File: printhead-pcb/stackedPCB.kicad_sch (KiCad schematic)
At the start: 17 parts, among them J13 Steckverbinder_Male_1, J14 Steckverbinder_Male_2, J15 Steckverbinder_Female_2, J16 Steckverbinder_Male_3, J17 Steckverbinder_Female_3

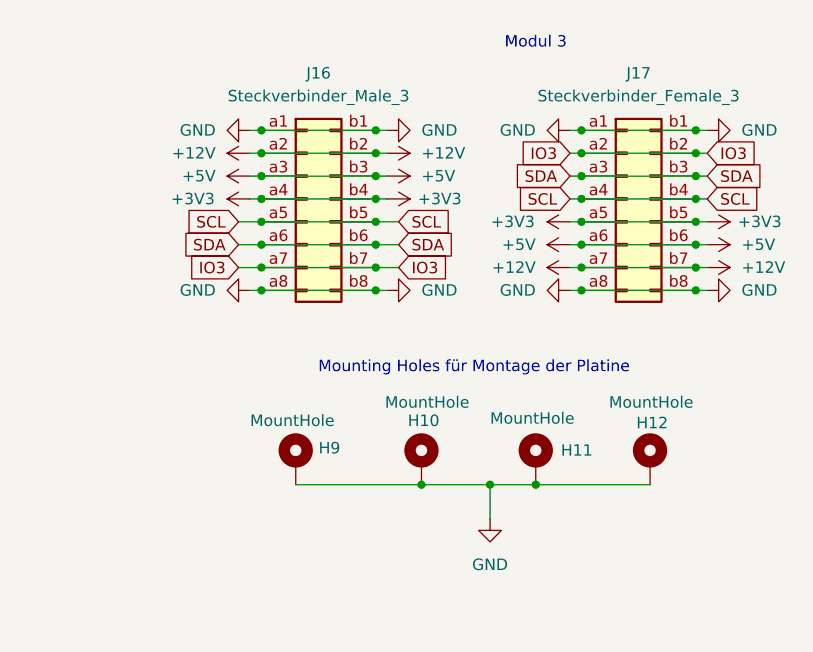
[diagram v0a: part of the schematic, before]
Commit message: rearanged the text for module 3
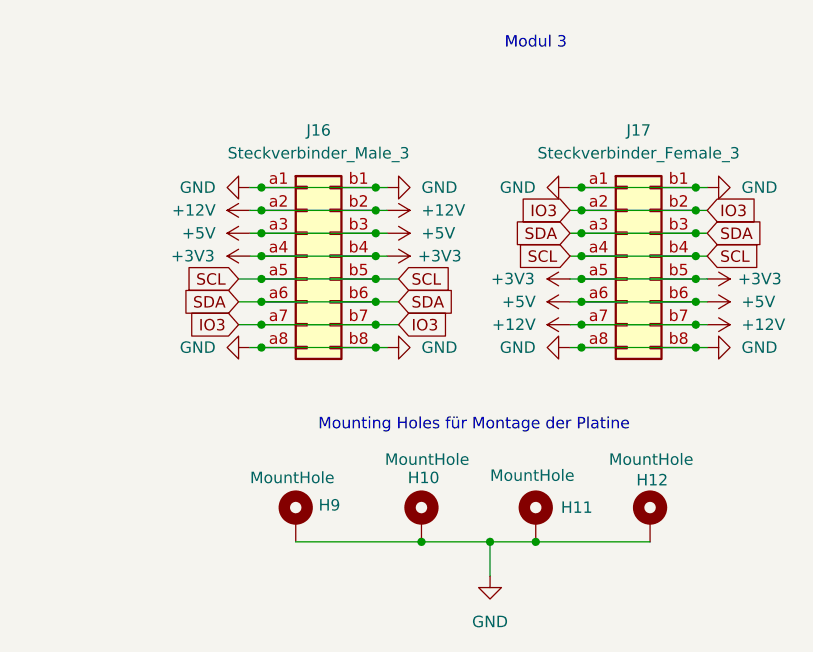
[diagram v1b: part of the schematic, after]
